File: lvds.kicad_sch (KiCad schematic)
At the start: 30 parts, among them J15 Conn_FFC_Amphenol_62684-40210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

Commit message: [#54231] Add initial power supply for LVDS display
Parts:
- added C? (x3): C_1u_25V_0402, antmicro-footprints:C_0402_1005Metric, symbol antmicroCapacitors0402:C_1u_25V_0402
- added C?: C_2n2_0402, antmicro-footprints:C_0402_1005Metric, symbol antmicroCapacitors0402:C_2n2_0402
- added C?: C_1n_0402, antmicro-footprints:C_0402_1005Metric, symbol antmicroCapacitors0402:C_1n_0402
- added C? (x4): C_330n_0603, antmicro-footprints:C_0603_1608Metric, symbol antmicroCapacitors0603:C_330n_0603
- added C? (x6): C_100n_0402, antmicro-footprints:C_0402_1005Metric, symbol antmicroCapacitors0402:C_100n_0402
- added C? (x4): C_10u_25V_0603, antmicro-footprints:C_0603_1608Metric, symbol antmicroCapacitors0603:C_10u_25V_0603
- added C?: C_10n_0402, antmicro-footprints:C_0402_1005Metric, symbol antmicroCapacitors0402:C_10n_0402
- added C?: C_22u_16V_0603, antmicro-footprints:C_0603_1608Metric, symbol antmicroCapacitors0603:C_22u_16V_0603
- added C? (x2): C_22p_0402, antmicro-footprints:C_0402_1005Metric, symbol antmicroCapacitors0402:C_22p_0402
- added C? (x2): C_220n_16V_0402, antmicro-footprints:C_0402_1005Metric, symbol antmicroCapacitors0402:C_220n_16V_0402
- added D? (x2): BAT54S-E3-08, antmicro-footprints:SOT-23-3, symbol antmicroDiodesRectifiersSingle:BAT54S-E3-08
- added D?: PMEG3010CE_SOD323, antmicro-footprints:D_SOD-323F, symbol antmicroDiodesRectifiersSingle:PMEG3010CE_SOD323
- added L?: L_27u_2A_Bourns-SRP6540, antmicro-footprints:L_Bourns-SRP6540, symbol antmicroFixedInductors:L_27u_2A_Bourns-SRP6540
- added L?: L_3u3_2.5A_1008, antmicro-footprints:L_1008_2520Metric, symbol antmicroFixedInductors:L_3u3_2.5A_1008
- added Q? (x2): SSM3J332R, antmicro-footprints:SOT-23-3, symbol antmicroTransistorsFETsMOSFETsSingle:SSM3J332R
- added Q?: BSS138-7-F, antmicro-footprints:SOT-23-3, symbol antmicroTransistorsFETsMOSFETsSingle:BSS138-7-F
- added R?: R_330k_0402, antmicro-footprints:R_0402_1005Metric, symbol antmicroResistors0402:R_330k_0402
- added R?: R_820k_0402, antmicro-footprints:R_0402_1005Metric, symbol antmicroResistors0402:R_820k_0402
- added R? (x5): R_0R_22.4A_0603, antmicro-footprints:R_0603_1608Metric, symbol antmicroResistors0603:R_0R_22.4A_0603
- added R? (x2): R_110k_0402, antmicro-footprints:R_0402_1005Metric, symbol antmicroResistors0402:R_110k_0402
- added R?: R_10k_0402, antmicro-footprints:R_0402_1005Metric, symbol antmicroResistors0402:R_10k_0402
- added R?: R_1M_0402, antmicro-footprints:R_0402_1005Metric, symbol antmicroResistors0402:R_1M_0402
- added R? (x3): R_100k_0402, antmicro-footprints:R_0402_1005Metric, symbol antmicroResistors0402:R_100k_0402
- added R?: R_100R_0402, antmicro-footprints:R_0402_1005Metric, symbol antmicroResistors0402:R_100R_0402
- added R?: R_510k_0402, antmicro-footprints:R_0402_1005Metric, symbol antmicroResistors0402:R_510k_0402
- added R?: R_20R_0603, antmicro-footprints:R_0603_1608Metric, symbol antmicroResistors0603:R_20R_0603
- added R?: R_1R2_0603, antmicro-footprints:R_0603_1608Metric, symbol antmicroResistors0603:R_1R2_0603
- added R?: R_120k_0402, antmicro-footprints:R_0402_1005Metric, symbol antmicroResistors0402:R_120k_0402
- added R?: R_0R_0402, antmicro-footprints:R_0402_1005Metric, symbol antmicroResistors0402:R_0R_0402
- added R?: R_680k_0402, antmicro-footprints:R_0402_1005Metric, symbol antmicroResistors0402:R_680k_0402
- added R?: R_590k_0402, antmicro-footprints:R_0402_1005Metric, symbol antmicroResistors0402:R_590k_0402
- added R?: R_1M5_0402, antmicro-footprints:R_0402_1005Metric, symbol antmicroResistors0402:R_1M5_0402
- added TP?: TP_0.75mm_SMD, antmicro-footprints:TP_SMD_0.75mm, symbol antmicroTestPoints:TP_0.75mm_SMD
- added U?: MPQ7235GQBE, antmicro-footprints:QFN-13_2.5x3mm, symbol antmicroPMICLEDDrivers:MPQ7235GQBE
- added U?: TPS65150PWP, antmicro-footprints:HTSSOP-24_W4.4mm_P0.65mm, symbol antmicroPMICVoltageRegulatorsDCDCSwitchingRegulators:TPS65150_HTSSOP
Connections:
- net +3V3: now also R?.1
- net -6V: now also R?.1
- net 18V: now also R?.2
- net 3V9: now also R?.2
- net 9V6: now also R?.2, R?.2
- net GND: now also C?.1, C?.1, C?.1, C?.1, C?.1, C?.1, C?.1, C?.1, C?.1, C?.1, C?.1, C?.1, C?.1, C?.1, C?.1, C?.1, C?.1, C?.1, C?.1, D?.2, Q?.2 (S), R?.1, R?.1, R?.1, R?.1, R?.2, U?.11 (GND), U?.12 (GND), U?.13 (GND), U?.19 (AGND), U?.25 (EP), U?.7 (PGND), U?.8 (GND), U?.8 (PGND)
- net VLED+: now also R?.2
- net VLED-: now also R?.2, R?.2
- new net: C?.2, Q?.3 (D), R?.1
- new net: R?.1, U?.6 (FB)
- new net: C?.2, R?.1, R?.2, U?.11 (IN)
- new net: C?.2, D?.1, R?.2, R?.2
- new net: C?.1, U?.17 (DRVP)
- new net: C?.2, D?.3
- new net: C?.1, L?.1, U?.9 (SW)
- new net: C?.2, R?.2
- new net: C?.1, R?.1, R?.1, U?.1 (FB)
- new net: C?.2, C?.2, C?.2, C?.2, C?.2, D?.1, D?.K, Q?.2 (S), R?.2, R?.2, U?.9 (SUP)
- new net: C?.2, D?.2, R?.2, U?.16 (CPI)
- new net: C?.1, D?.3
- new net: C?.2, U?.18 (DRVN)
- new net: R?.1, R?.2, U?.12 (FBP)
- new net: C?.2, Q?.1 (G), R?.2, R?.2
- new net: C?.2, L?.2, R?.1
- new net: C?.1, Q?.1 (G), R?.1, R?.2
- new net: C?.2, U?.7 (V_{CC})
- new net: R?.1, U?.15 (VGH)
- new net: Q?.1 (G), Q?.3 (D), R?.1
- new net: R?.1, U?.10 (BST)
- new net: TP?.1, U?.4 (~{FAULT})
- new net: D?.A, L?.2, U?.5 (SW), U?.6 (SW)
- new net: C?.2, R?.1, U?.20 (REF)
- new net: R?.1, R?.2, U?.21 (FBN)
- new net: C?.2, R?.1, U?.10 (VCOM)
- new net: R?.1, U?.23 (GD)
- new net: C?.2, L?.1, Q?.3 (D), U?.4 (VIN)
- new net +5V: C?.2, Q?.2 (S), R?.2, R?.2
- new net ADJ: C?.2, U?.14 (ADJ)
- new net COMP: C?.2, U?.22 (COMP)
- new net DIM: R?.1, U?.5 (DIM)
- new net DLY1: C?.2, U?.2 (DLY1)
- new net DLY2: C?.2, U?.3 (DLY2)
- new net FDLY: C?.1, U?.24 (FDLY)
- new net FLK: R?.1, U?.13 (CTRL)
- new net VCC: C?.2, C?.2, R?.2, U?.1 (IN), U?.2 (IN)
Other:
- note added: "(Note):backlight not connected to any power-sequencer"
- note added: "Backlight driver"
- note added: "Backlight should be set to 180mA CC (voltage from 8.55 to 10.65)"
- note added: "LCD datasheet pg.6"
- note added: "LCD datasheet pg.7"
- note added: "Powering sequence VDD(3v3) -> VGL(-6V) -> VGH -> Logic signal -> Backlight"
- note added: "Required voltages: Voltage - Current - Pin from TPS6515 -3V9- 45mA - TPS VCOM -9V6- 37mA - TPS VS - (-6V)- 1mA - TPS VGL -18V- 1mA - TPS VGH - 9V6- 180mA - DCDC - backlight"
- note added: "TFT screen power supply"
- note added: "Vcom=(R2/(R1+R2))*Vin"
- note added: "Vo=(1+R1/R2)*1.146"
- note added: "Vo=(1+R1/R2)*1.214"
- note added: "Vo=-(R1/R2)*1.213"

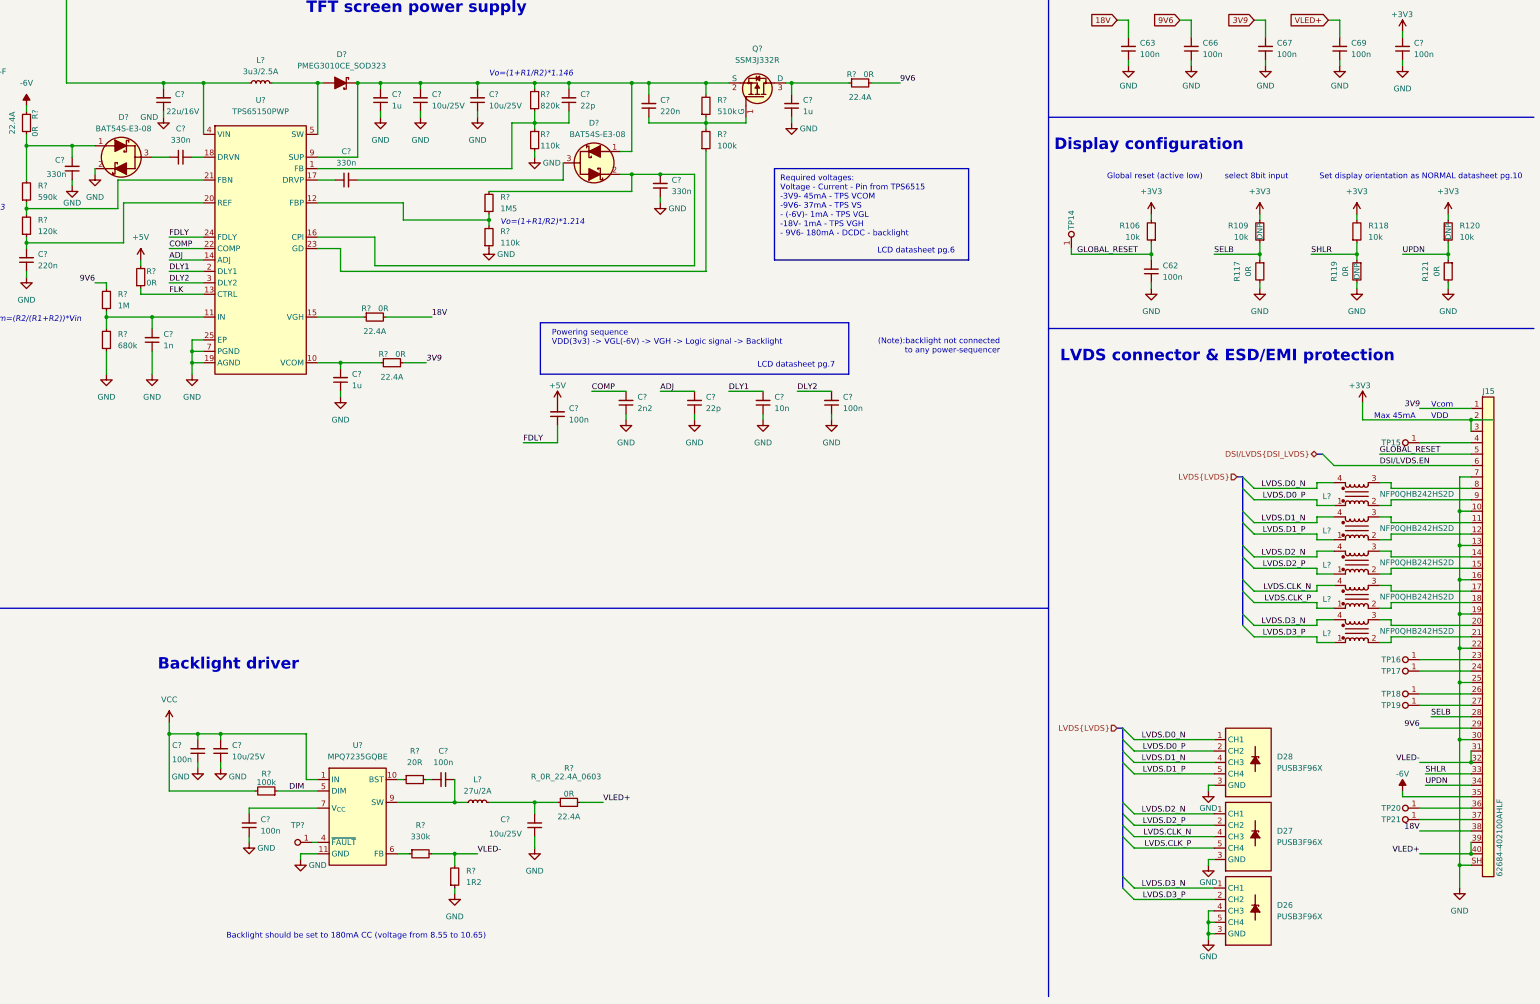
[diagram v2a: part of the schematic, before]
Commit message: [#54231] Clean backlight driver sch
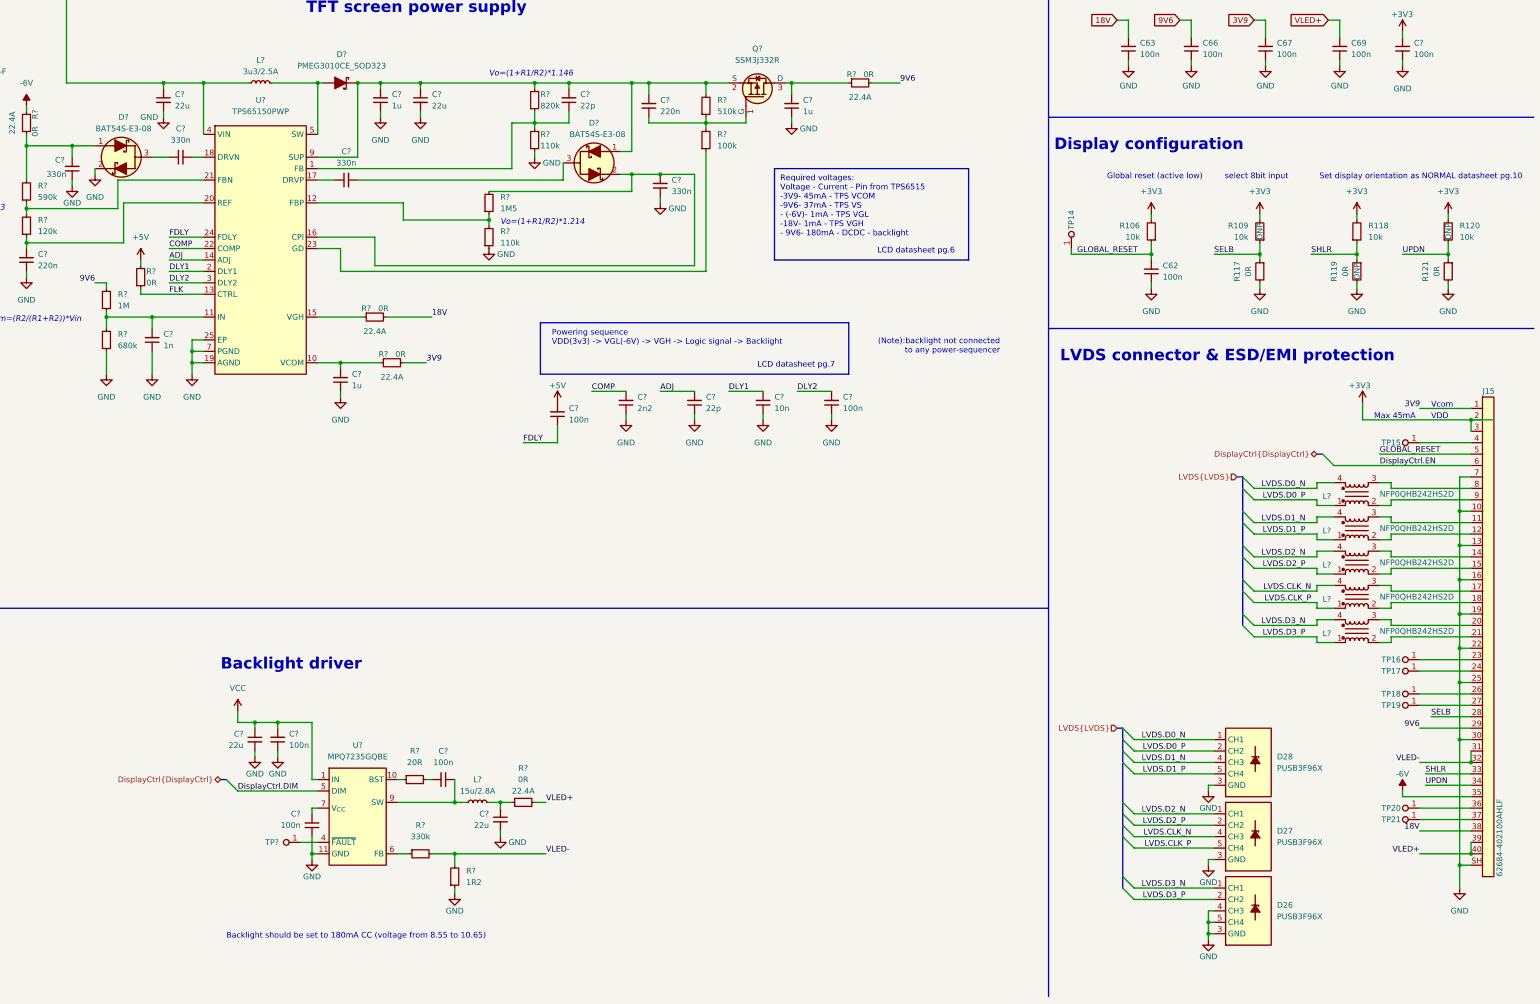
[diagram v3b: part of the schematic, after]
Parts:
- removed C? (x4): C_10u_25V_0603, antmicro-footprints:C_0603_1608Metric, symbol antmicroCapacitors0603:C_10u_25V_0603
- removed C?: C_22u_16V_0603, antmicro-footprints:C_0603_1608Metric, symbol antmicroCapacitors0603:C_22u_16V_0603
- removed L?: L_27u_2A_Bourns-SRP6540, antmicro-footprints:L_Bourns-SRP6540, symbol antmicroFixedInductors:L_27u_2A_Bourns-SRP6540
- removed R?: R_100k_0402, antmicro-footprints:R_0402_1005Metric, symbol antmicroResistors0402:R_100k_0402
- added C? (x4): C_22u_25V_0805, antmicro-footprints:C_0805_2012Metric, symbol antmicroCapacitorsmisc:C_22u_25V_0805
- added L?: L_15u_2.8A_Coilcraft-XAL4040, antmicro-footprints:L_Coilcraft-XAL4040, symbol antmicroFixedInductors:L_15u_2.8A_Coilcraft-XAL4040
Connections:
- net GND: now also C?.2, C?.2, C?.2, C?.2
- net VCC: now also C?.1
- net at C?.1, U?.9 (SW): now also L?.1
- net at C?.2, C?.2, C?.2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: now also C?.1
- net at R?.1: now also C?.1, L?.2
- net at L?.1, Q?.3 (D), U?.4 (VIN): now also C?.1
- net DIM renamed DisplayCtrl.DIM
- net DSI/LVDS.EN renamed DisplayCtrl.EN
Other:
- moved on the sheet: C?, R?, TP?
